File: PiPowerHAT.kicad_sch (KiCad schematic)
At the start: 40 parts, among them J1 2444, J2 Conn_01x03, J3 Conn_01x02, J5 Conn_01x06, J6 Raspberry_Pi_2_3, J7 Conn_02x03_Odd_Even, Q1 AO3401A, Q2 MMDT5401, Q3 DMG2305UX-13, U1 XL4015, U2 CAT24C32

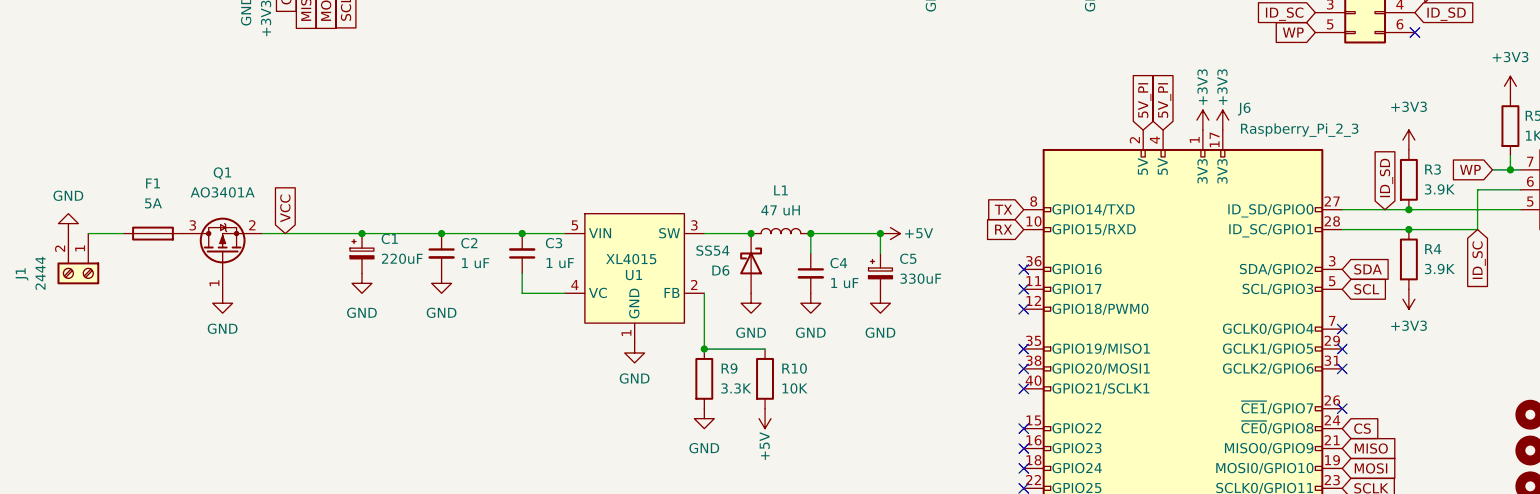
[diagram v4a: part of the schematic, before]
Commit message: cleanup and added proper JLC number for fuseholder
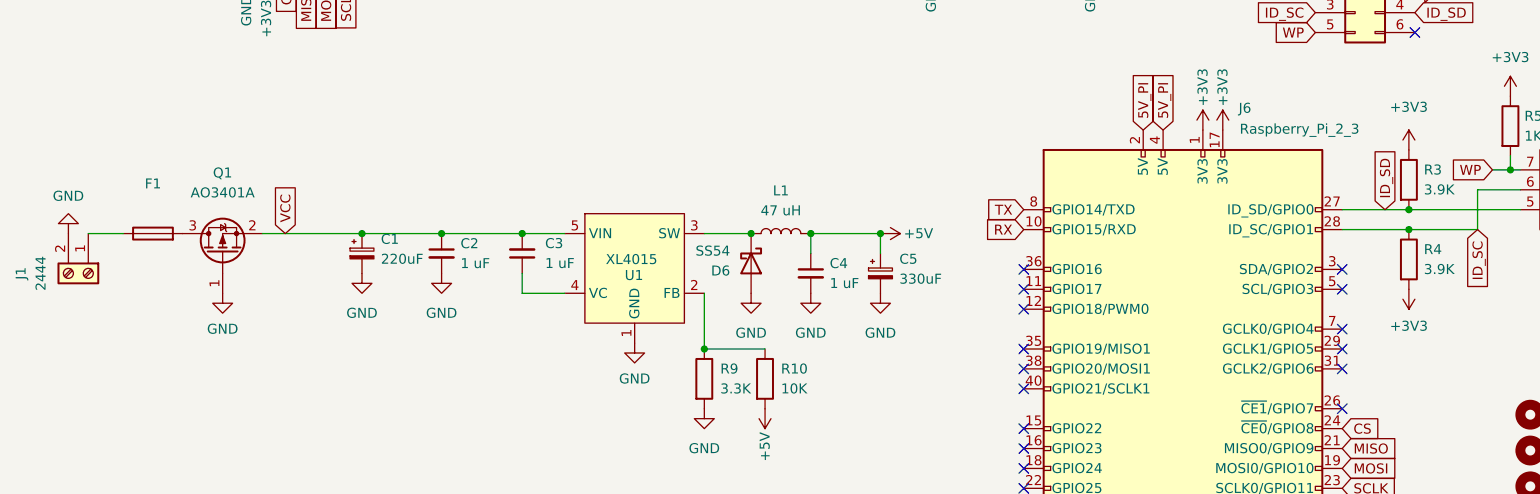
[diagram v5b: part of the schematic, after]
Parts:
- F1: value 5A -> (none); footprint Fuse:Fuseholder_Littelfuse_Nano2_154x -> (none); Farnell 2292904 -> (none); JLC (none) -> C206916
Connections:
- net SCL: no longer names the net of J6.5 (SCL/GPIO3)
- net SDA: no longer names the net of J6.3 (SDA/GPIO2)
- no-connect marks 19 -> 21
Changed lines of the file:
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@@
   (no_connect (at 141.986 100.203))
   (no_connect (at 141.986 102.743))
+  (no_connect (at 182.626 100.203))
+  (no_connect (at 182.626 102.743))
   (no_connect (at 191.897 69.977))
   (wire (pts (xy 139.065 52.959) (xy 150.495 52.959))
@@
     )
   )
-  (global_label "SCL" (shape input) (at 182.626 102.743 0) (fields_autoplaced)
-    (effects (font (size 1.27 1.27)) (justify left))
-    (property "Intersheet References" "${INTERSHEET_REFS}" (id 0) (at 188.5467 102.6636 0)
-      (effects (font (size 1.27 1.27)) (justify left) hide)
-    )
-  )
   (global_label "5V_PI" (shape input) (at 150.495 42.799 90) (fields_autoplaced)
     (effects (font (size 1.27 1.27)) (justify left))
@@
     (effects (font (size 1.27 1.27)) (justify left))
     (property "Intersheet References" "${INTERSHEET_REFS}" (id 0) (at 199.632 67.3576 0)
-      (effects (font (size 1.27 1.27)) (justify left) hide)
-    )
-  )
-  (global_label "SDA" (shape input) (at 182.626 100.203 0) (fields_autoplaced)
-    (effects (font (size 1.27 1.27)) (justify left))
-    (property "Intersheet References" "${INTERSHEET_REFS}" (id 0) (at 188.6072 100.1236 0)
       (effects (font (size 1.27 1.27)) (justify left) hide)
     )
@@
     (in_bom yes) (on_board yes) (fields_autoplaced)
     (property "Reference" "F1" (id 0) (at 30.861 89.281 90))
-    (property "Value" "5A" (id 1) (at 30.861 91.821 90))
-    (property "Footprint" "Fuse:Fuseholder_Littelfuse_Nano2_154x" (id 2) (at 30.861 97.409 90)
+    (property "Value" "" (id 1) (at 30.861 91.821 90))
+    (property "Footprint" "" (id 2) (at 30.861 97.409 90)
       (effects (font (size 1.27 1.27)) hide)
     )
@@
       (effects (font (size 1.27 1.27)) hide)
     )
-    (property "Farnell" "2292904" (id 4) (at 30.861 95.631 90)
-      (effects (font (size 1.27 1.27)) hide)
-    )
+    (property "JLC" "C206916" (id 4) (at 30.861 95.631 90)
+      (effects (font (size 1.27 1.27)) hide)
+    )

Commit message: Layout V1 complete
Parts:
- F1: value (none) -> 5A; footprint (none) -> Fuse:Fuseholder_Littelfuse_Nano2_154x
- J3: value Conn_01x02 -> (none); footprint Connector_JST:JST_XH_B2B-XH-AM_1x02_P2.50mm_Vertical -> (none)
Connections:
- net +3V3: no longer J6.1 (3V3)
- no-connect marks 21 -> 22
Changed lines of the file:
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@@
   (junction (at 74.549 52.832) (diameter 0) (color 0 0 0 0)
   )
+  (no_connect (at 164.846 82.423))
   (no_connect (at 141.986 133.223))
   (no_connect (at 141.986 125.603))
@@
       (effects (font (size 1.27 1.27)) (justify right))
     )
-    (property "Value" "Conn_01x02" (id 1) (at 77.216 40.3859 90)
+    (property "Value" "" (id 1) (at 77.216 40.3859 90)
       (effects (font (size 1.27 1.27)) (justify right))
     )
-    (property "Footprint" "Connector_JST:JST_XH_B2B-XH-AM_1x02_P2.50mm_Vertical" (id 2) (at 72.009 39.116 0)
+    (property "Footprint" "" (id 2) (at 72.009 39.116 0)
       (effects (font (size 1.27 1.27)) hide)
     )
@@
     )
     (property "Datasheet" "" (id 3) (at 164.846 148.463 0)
-      (effects (font (size 1.27 1.27)) hide)
-    )
-    (pin "1")
-  )
-  (symbol (lib_id "power:+3V3") (at 164.846 82.423 0) (unit 1)
-    (in_bom yes) (on_board yes)
-    (property "Reference" "#PWR024" (id 0) (at 164.846 86.233 0)
-      (effects (font (size 1.27 1.27)) hide)
-    )
-    (property "Value" "+3V3" (id 1) (at 164.846 76.962 90))
-    (property "Footprint" "" (id 2) (at 164.846 82.423 0)
-      (effects (font (size 1.27 1.27)) hide)
-    )
-    (property "Datasheet" "" (id 3) (at 164.846 82.423 0)
       (effects (font (size 1.27 1.27)) hide)
     )
@@
     (in_bom yes) (on_board yes) (fields_autoplaced)
     (property "Reference" "F1" (id 0) (at 30.861 89.281 90))
-    (property "Value" "" (id 1) (at 30.861 91.821 90))
-    (property "Footprint" "" (id 2) (at 30.861 97.409 90)
+    (property "Value" "5A" (id 1) (at 30.861 91.821 90))
+    (property "Footprint" "Fuse:Fuseholder_Littelfuse_Nano2_154x" (id 2) (at 30.861 97.409 90)
       (effects (font (size 1.27 1.27)) hide)
     )
@@
       (reference "#PWR023") (unit 1) (value "GND") (footprint "")
     )
-    (path "/553b4831-05b8-4441-855c-40148b2c48fb"
-      (reference "#PWR024") (unit 1) (value "+3V3") (footprint "")
-    )
     (path "/51d4578a-55f0-4e98-8752-c651b3a2d606"
       (reference "#PWR025") (unit 1) (value "GND") (footprint "")
@@
     )
     (path "/12571268-be51-457b-85b9-1c2e7398dddd"
-      (reference "J3") (unit 1) (value "Conn_01x02") (footprint "Connector_JST:JST_XH_B2B-XH-AM_1x02_P2.50mm_Vertical")
+      (reference "J3") (unit 1) (value "Conn_01x02") (footprint "Connector_JST:JST_XH_S2B-XH-A_1x02_P2.50mm_Horizontal")
     )
     (path "/b0d40fbf-eaab-4638-8138-e4a813009096"

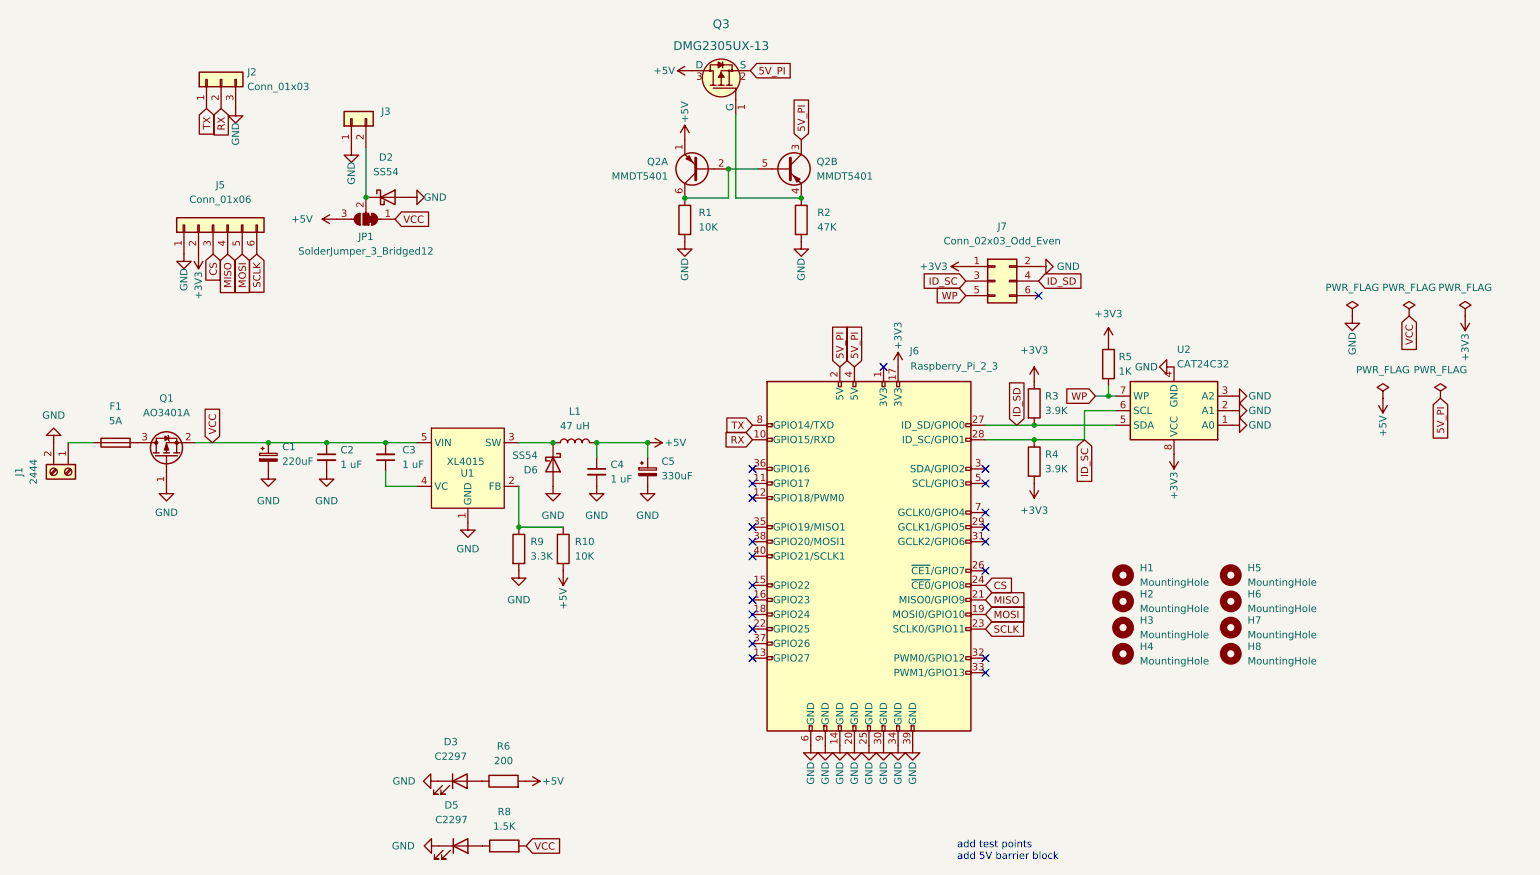
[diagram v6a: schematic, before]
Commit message: Adding panelization between breakouts. Updated layout and component position.
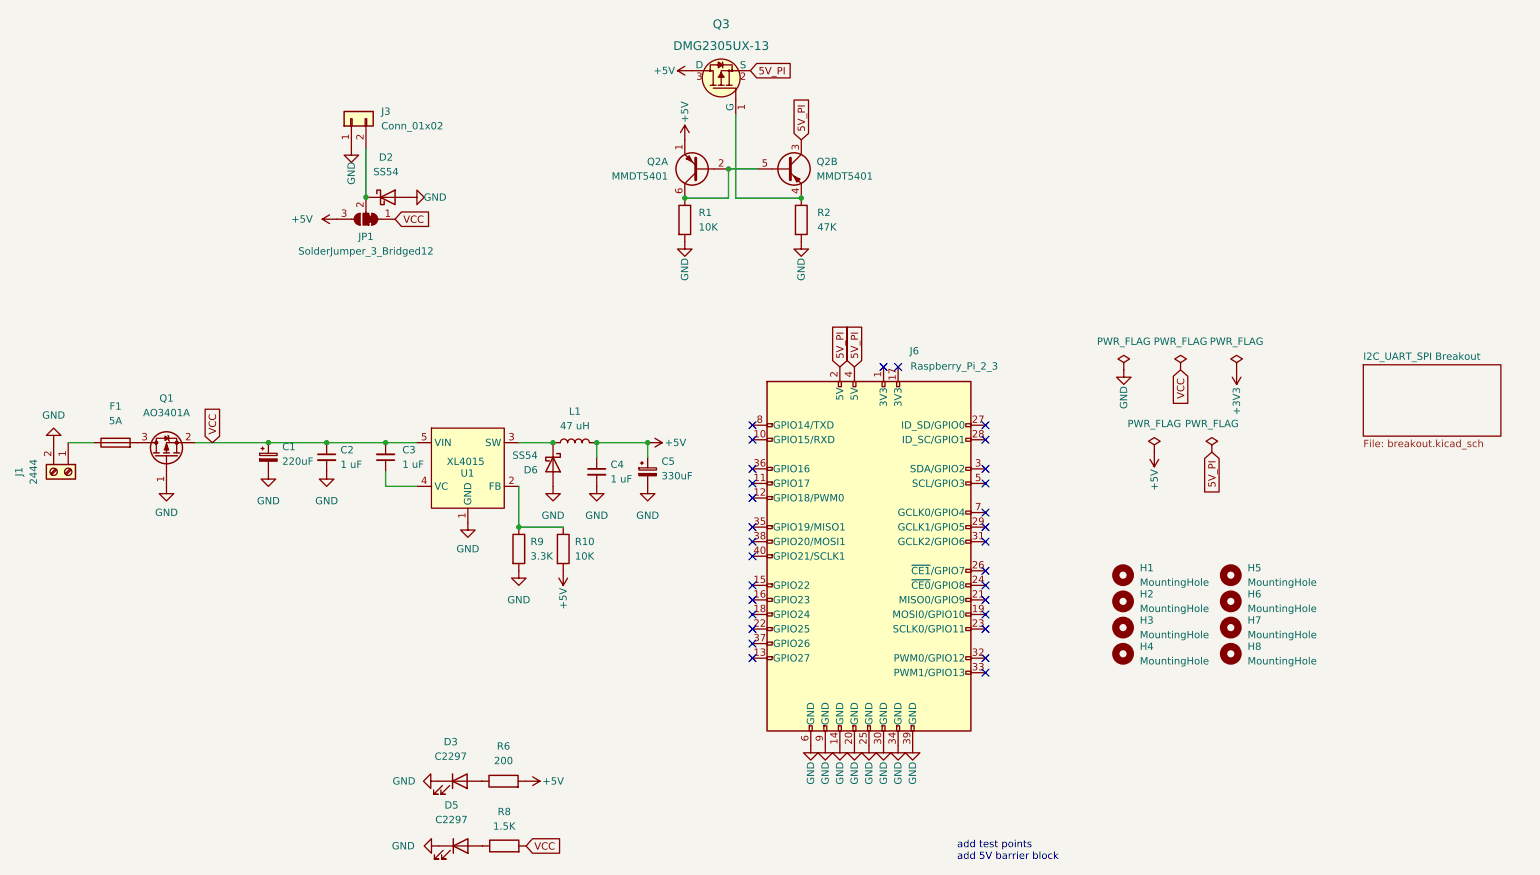
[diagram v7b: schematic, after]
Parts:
- removed J2: Conn_01x03, Connector_PinHeader_2.54mm:PinHeader_1x03_P2.54mm_Vertical_SMD_Pin1Left, symbol Connector_Generic:Conn_01x03
- removed J5: Conn_01x06, Connector_PinHeader_2.54mm:PinHeader_1x06_P2.54mm_Vertical_SMD_Pin1Left, symbol Connector_Generic:Conn_01x06
- removed J7: Conn_02x03_Odd_Even, Connector_PinHeader_2.54mm:PinHeader_2x03_P2.54mm_Vertical_SMD, symbol Connector_Generic:Conn_02x03_Odd_Even
- removed R3, R4: 3.9K, Resistor_SMD:R_0402_1005Metric, symbol Device:R
- removed R5: 1K, Resistor_SMD:R_0402_1005Metric, symbol Device:R
- removed U2: CAT24C32, Package_SO:SOIC-8_3.9x4.9mm_P1.27mm, symbol Memory_EEPROM:CAT24C128
- J3: value (none) -> Conn_01x02; footprint (none) -> Connector_JST:JST_XH_B2B-XH-AM_1x02_P2.50mm_Vertical
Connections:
- net +3V3: no longer J6.17 (3V3)
- net CS: no longer names the net of J6.24 (~{CE0}/GPIO8)
- net ID_SC: no longer names the net of J6.28 (ID_SC/GPIO1)
- net ID_SD: no longer names the net of J6.27 (ID_SD/GPIO0)
- net MISO: no longer names the net of J6.21 (MISO0/GPIO9)
- net MOSI: no longer names the net of J6.19 (MOSI0/GPIO10)
- net RX: no longer names the net of J6.10 (GPIO15/RXD)
- net SCLK: no longer names the net of J6.23 (SCLK0/GPIO11)
- net TX: no longer names the net of J6.8 (GPIO14/TXD)
- no-connect marks 22 -> 30
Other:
- added sheet I2C_UART_SPI Breakout (breakout.kicad_sch)

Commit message: remove breakout board and add +5V out
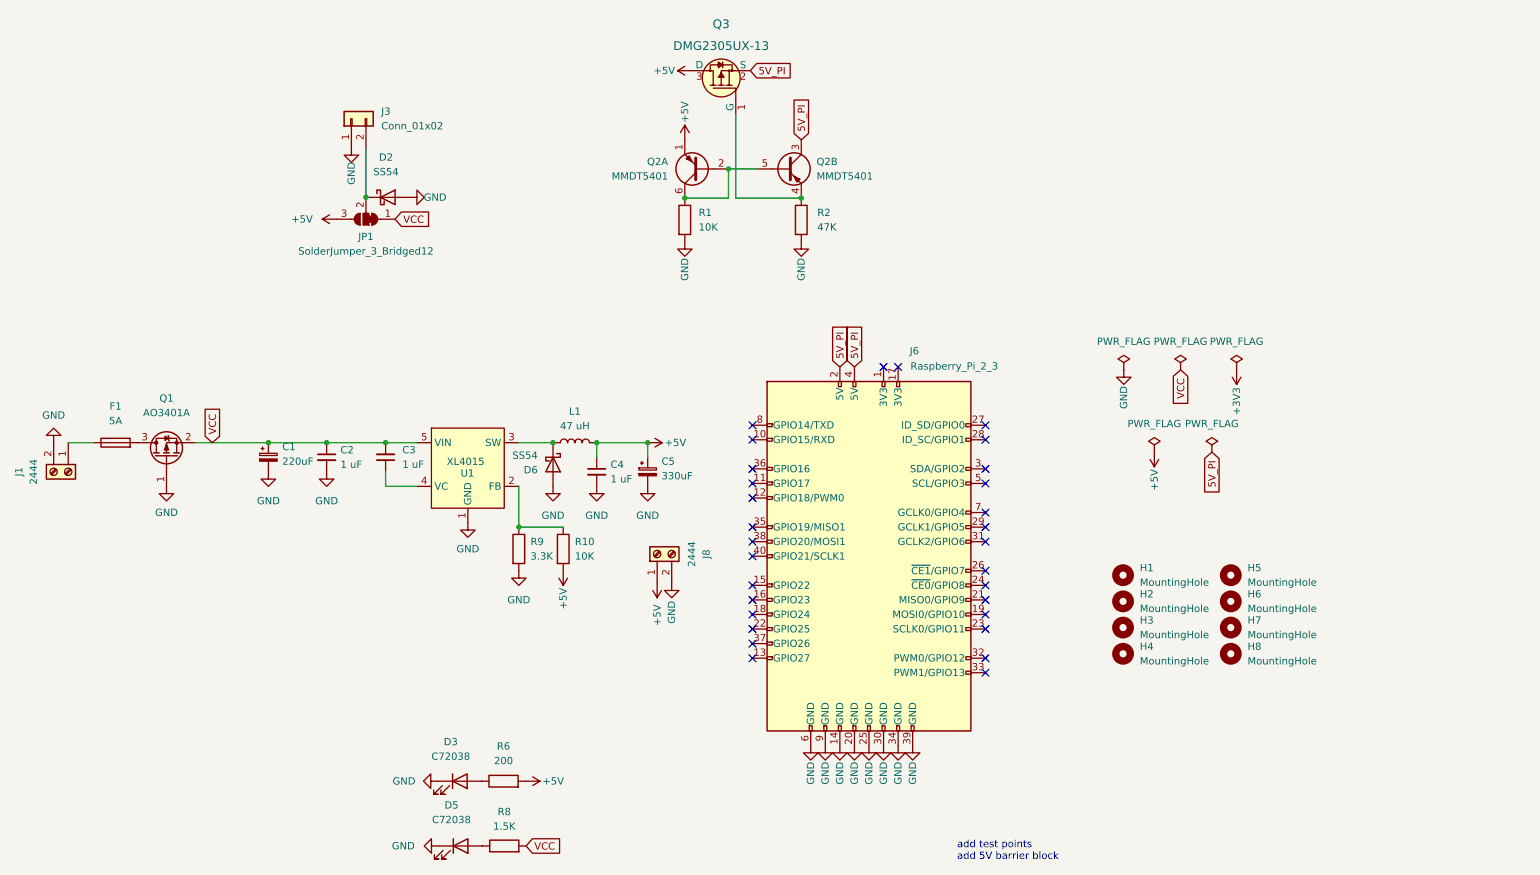
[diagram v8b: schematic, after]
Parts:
- added J8: 2444, TerminalBlock_4Ucon:TerminalBlock_4Ucon_1x02_P3.50mm_Horizontal, symbol Connector:Screw_Terminal_01x02
- D3, D5: value C2297 -> C72038; footprint LED_SMD:LED_0805_2012Metric -> LED_SMD:LED_0603_1608Metric
- J3: footprint Connector_JST:JST_XH_B2B-XH-AM_1x02_P2.50mm_Vertical -> Connector_JST:JST_XH_B2B-XH-A_1x02_P2.50mm_Vertical
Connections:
- net +5V: now also J8.1 (Pin_1)
- net GND: now also J8.2 (Pin_2)
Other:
- removed sheet I2C_UART_SPI Breakout
